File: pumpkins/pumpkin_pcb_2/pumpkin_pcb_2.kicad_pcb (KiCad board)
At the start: 2 copper layers, 6 parts, among them SW1 SMT_SPDT

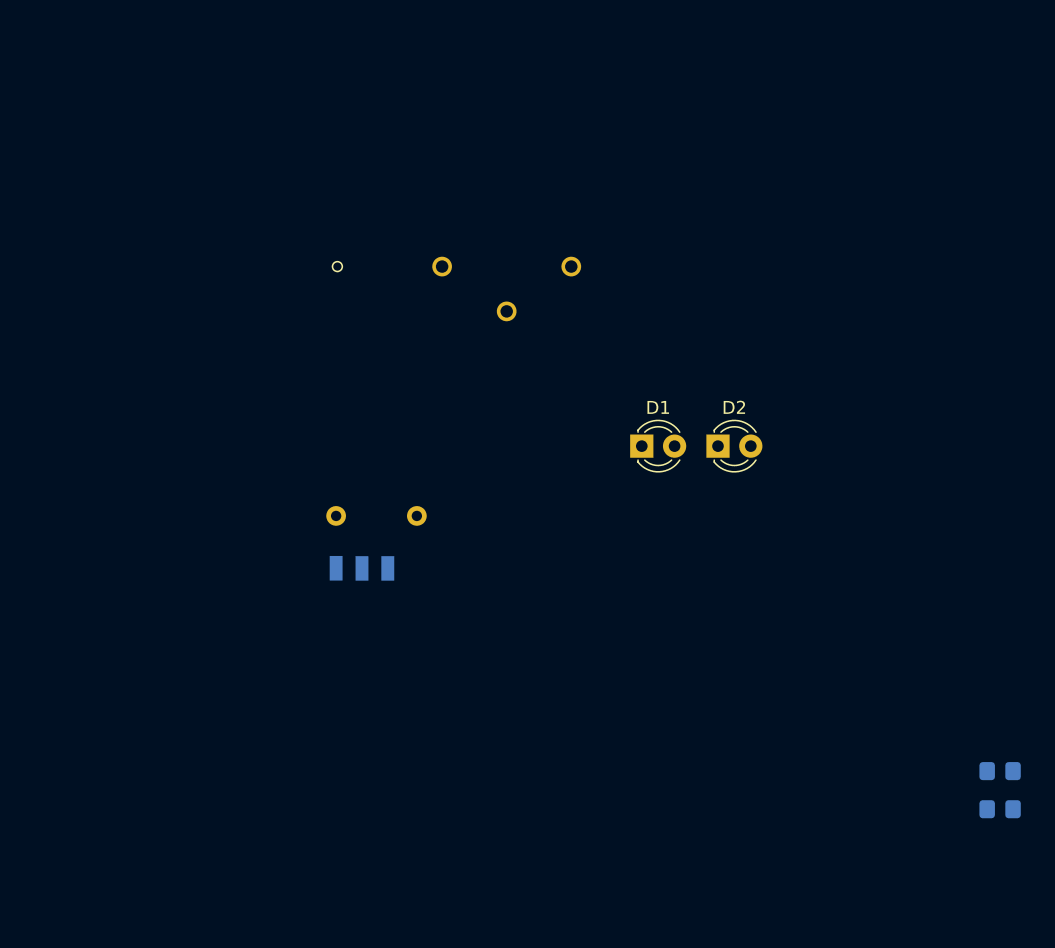
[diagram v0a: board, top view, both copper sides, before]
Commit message: Updating all PCBS, etc.
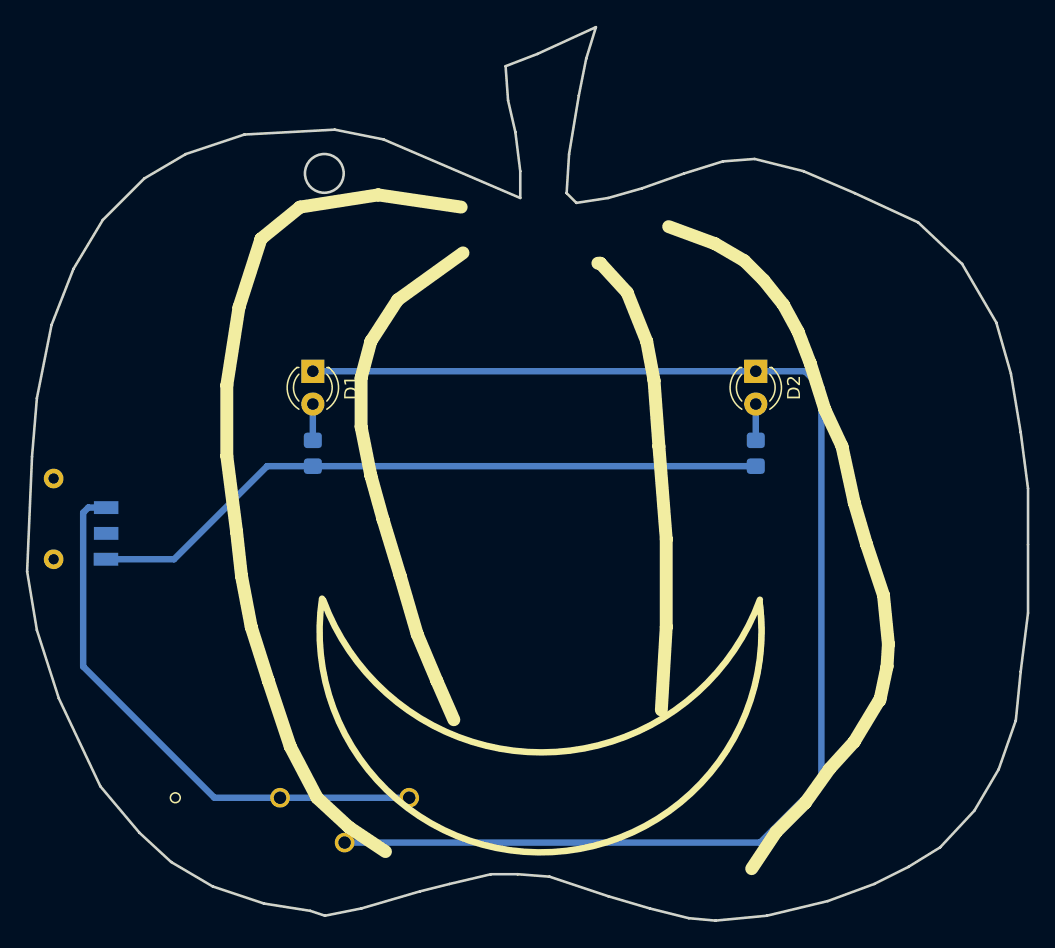
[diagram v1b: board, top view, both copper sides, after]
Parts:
- moved R1 59.9 mm to (117.0, 90.7), turned to 90 degrees
- moved BAT1 43.0 mm to (114.5, 117.3)
- moved R2 31.0 mm to (151.3, 90.7), turned to 90 degrees
- moved D1 26.1 mm to (117.0, 84.3), turned to 270 degrees
- moved SW1 22.8 mm to (99.2, 95.7), turned to 90 degrees
- moved D2 6.49 mm to (151.3, 84.3), turned to 270 degrees
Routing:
- net GND: track 0.00 -> 109.2 mm
- net Net-(R1-Pad1): track 0.00 -> 53.3 mm
- net VDD: track 0.00 -> 43.3 mm
- net Net-(D2-Pad2): track 0.00 -> 2.81 mm
- net Net-(D1-Pad2): track 0.00 -> 2.81 mm
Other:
- board outline added: 77.5 x 69.2 mm
- board text added: "+ Positive +"
